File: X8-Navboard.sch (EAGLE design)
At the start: 14 parts, among them U1 MS5803-14BA

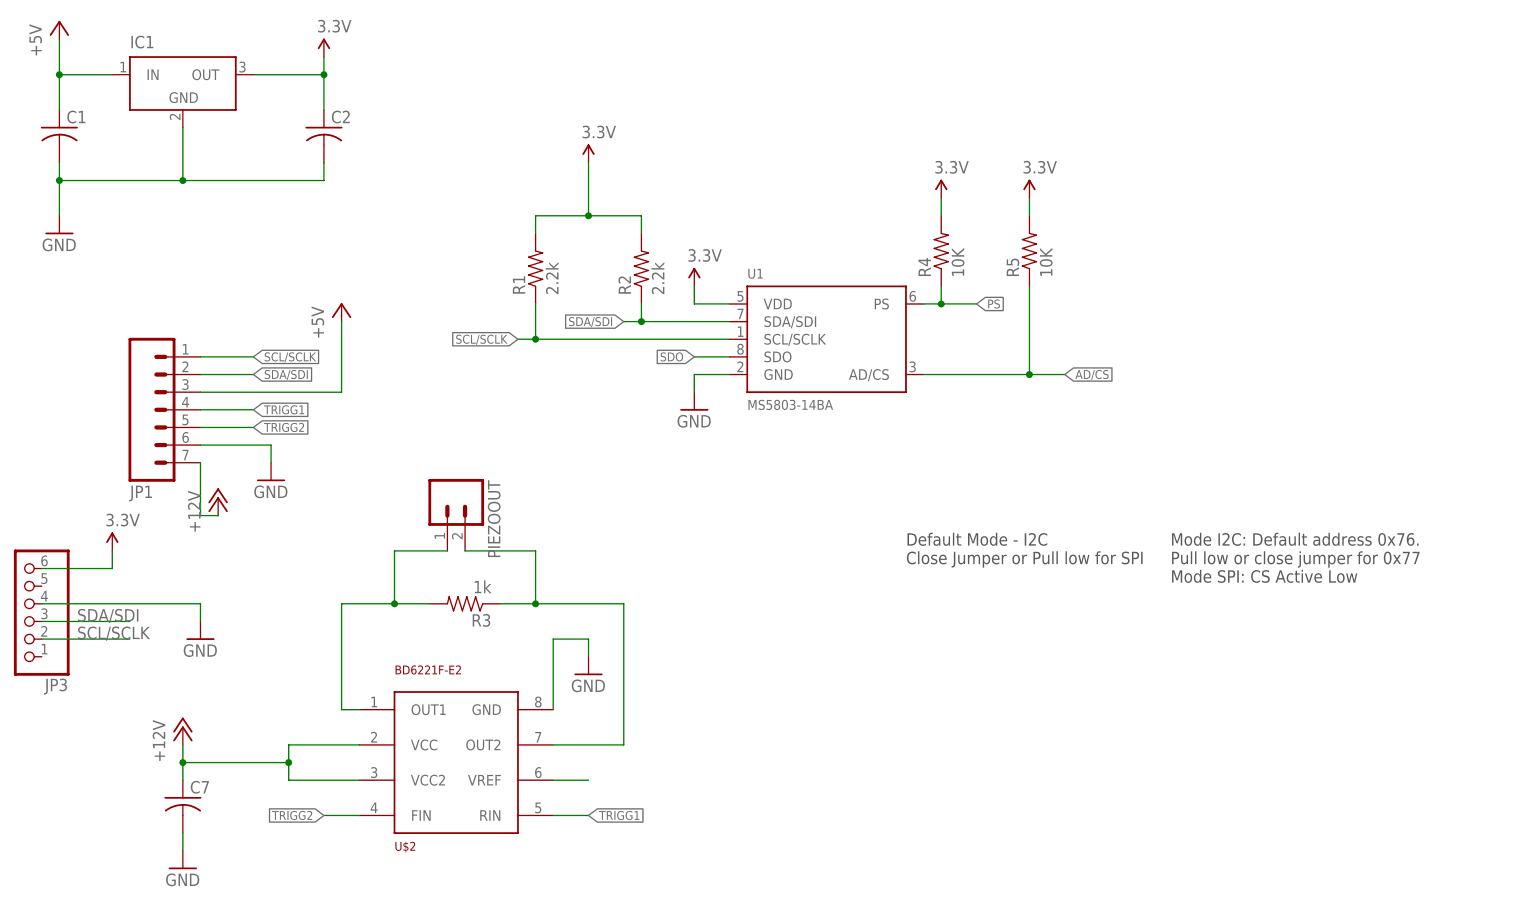
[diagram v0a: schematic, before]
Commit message: Finished the board layout for the nav board
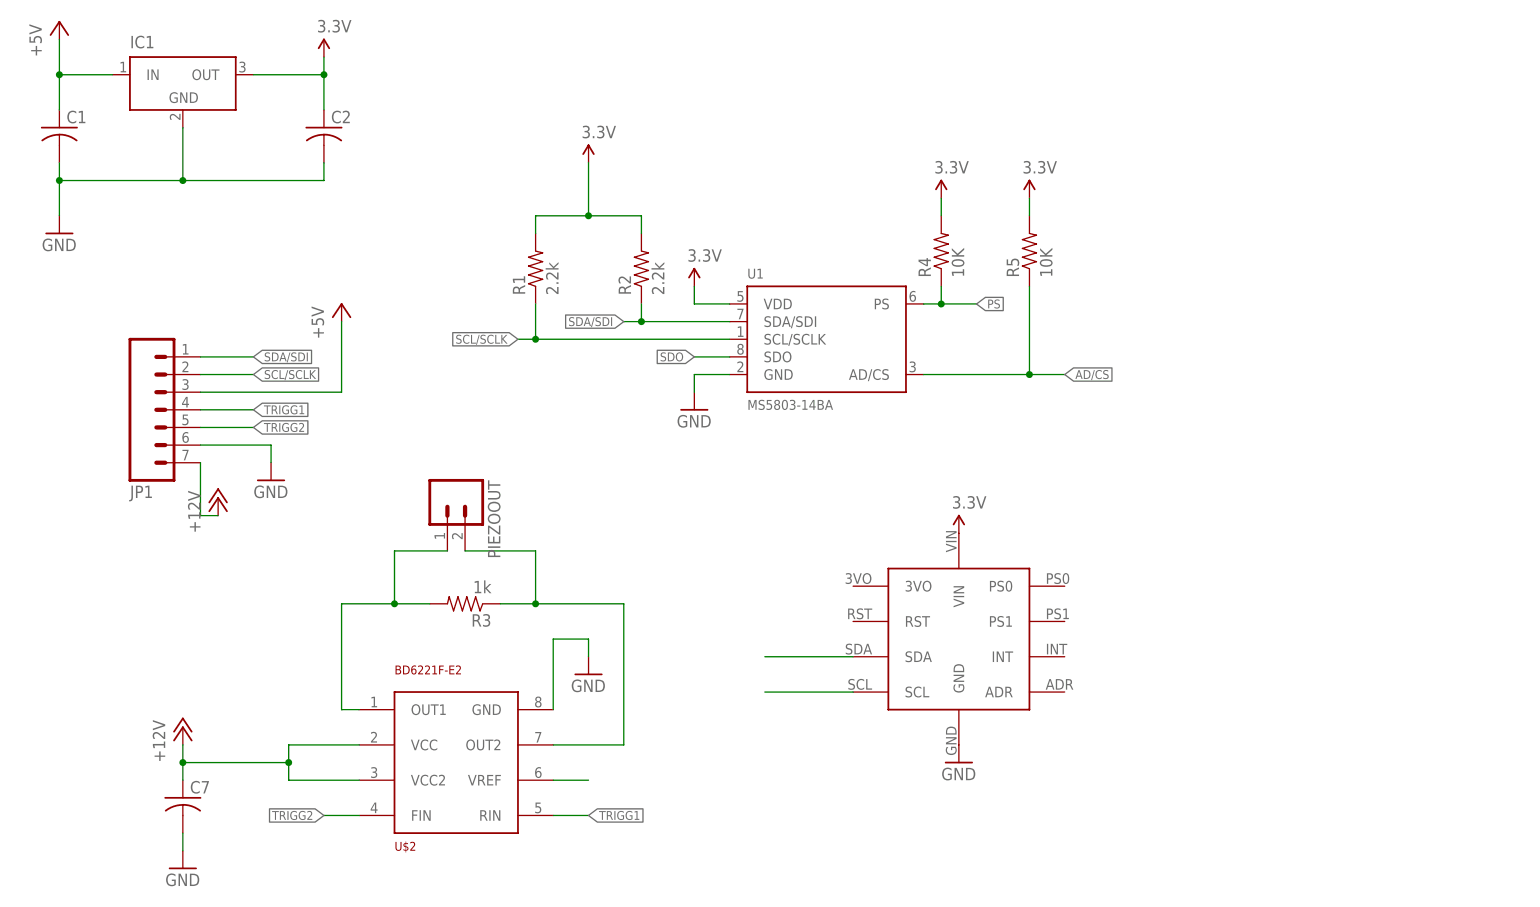
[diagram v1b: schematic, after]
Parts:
- removed JP3: (no value), pinhead:PINHD-1X6
- added U$1: BNO055_9DOF_BREAKOUT, Other:BNO055_9DOF_BREAKOUT
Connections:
- net 3.3V: now also U$1.VIN; no longer JP3.6
- net GND: now also U$1.GND; no longer JP3.4
- net SCL/SCLK: now also JP1.2, U$1.SCL; no longer JP1.1, JP3.2
- net SDA/SDI: now also JP1.1, U$1.SDA; no longer JP1.2, JP3.3
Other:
- note removed: "Default Mode - I2C Close Jumper or Pull low for SPI"
- note removed: "Mode I2C: Default address 0x76. Pull low or close jumper for 0x77 Mode SPI: CS Active Low"
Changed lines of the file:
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@@
 <part name="U$2" library="BNo-055" deviceset="BD6221F-E2" device=""/>
 <part name="PIEZOOUT" library="SparkFun-Connectors" deviceset="M02" device="LOCK_LONGPADS"/>
-<part name="SUPPLY9" library="SparkFun-Aesthetics" deviceset="3.3V" device=""/>
-<part name="GND10" library="SparkFun-Aesthetics" deviceset="GND" device=""/>
 <part name="P+1" library="supply1" deviceset="+5V" device=""/>
 <part name="P+2" library="supply1" deviceset="+5V" device=""/>
@@
 <part name="SUPPLY2" library="SparkFun-Aesthetics" deviceset="3.3V" device=""/>
 <part name="SUPPLY7" library="SparkFun-Aesthetics" deviceset="3.3V" device=""/>
-<part name="JP3" library="pinhead" deviceset="PINHD-1X6" device=""/>
+<part name="U$1" library="Other" deviceset="BNO055_9DOF_BREAKOUT" device=""/>
+<part name="SUPPLY3" library="SparkFun-Aesthetics" deviceset="3.3V" device=""/>
+<part name="GND5" library="SparkFun-Aesthetics" deviceset="GND" device=""/>
 </parts>
 <sheets>
 <sheet>
 <plain>
-<text x="157.48" y="86.36" size="1.778" layer="97" align="top-left">Default Mode - I2C
-Close Jumper or Pull low for SPI</text>
-<text x="195.58" y="86.36" size="1.778" layer="97" align="top-left">Mode I2C: Default address 0x76.
-Pull low or close jumper for 0x77
-Mode SPI: CS Active Low</text>
 </plain>
 <instances>
@@
 <instance part="U$2" gate="G$1" x="83.82" y="43.18"/>
 <instance part="PIEZOOUT" gate="G$1" x="91.44" y="91.44" rot="R270"/>
-<instance part="SUPPLY9" gate="G$1" x="43.18" y="83.82"/>
-<instance part="GND10" gate="1" x="55.88" y="71.12"/>
 <instance part="P+1" gate="1" x="35.56" y="160.02"/>
 <instance part="P+2" gate="1" x="76.2" y="119.38"/>
@@
 <instance part="SUPPLY2" gate="G$1" x="162.56" y="134.62"/>
 <instance part="SUPPLY7" gate="G$1" x="175.26" y="134.62"/>
-<instance part="JP3" gate="A" x="30.48" y="76.2" rot="R180"/>
+<instance part="U$1" gate="G$1" x="167.64" y="68.58"/>
+<instance part="SUPPLY3" gate="G$1" x="165.1" y="86.36"/>
+<instance part="GND5" gate="1" x="165.1" y="53.34"/>
 </instances>
 <busses>
@@
 </segment>
 <segment>
-<pinref part="JP3" gate="A" pin="6"/>
-<pinref part="SUPPLY9" gate="G$1" pin="3.3V"/>
-<wire x1="33.02" y1="81.28" x2="43.18" y2="81.28" width="0.1524" layer="91"/>
-<wire x1="43.18" y1="81.28" x2="43.18" y2="83.82" width="0.1524" layer="91"/>
+<pinref part="U$1" gate="G$1" pin="VIN"/>
+<pinref part="SUPPLY3" gate="G$1" pin="3.3V"/>
 </segment>
 </net>
@@
 </segment>
 <segment>
-<pinref part="JP3" gate="A" pin="4"/>
-<pinref part="GND10" gate="1" pin="GND"/>
-<wire x1="33.02" y1="76.2" x2="55.88" y2="76.2" width="0.1524" layer="91"/>
-<wire x1="55.88" y1="76.2" x2="55.88" y2="73.66" width="0.1524" layer="91"/>
+<pinref part="U$1" gate="G$1" pin="GND"/>
+<pinref part="GND5" gate="1" pin="GND"/>
 </segment>
 </net>
 <net name="SDA/SDI" class="0">
 <segment>
-<wire x1="45.72" y1="73.66" x2="33.02" y2="73.66" width="0.1524" layer="91"/>
-<label x="38.1" y="73.66" size="1.778" layer="95"/>
-<pinref part="JP3" gate="A" pin="3"/>
-</segment>
-<segment>
-<pinref part="JP1" gate="G$1" pin="2"/>
-<wire x1="55.88" y1="109.22" x2="63.5" y2="109.22" width="0.1524" layer="91"/>
-<label x="63.5" y="109.22" size="1.27" layer="95" xref="yes"/>
+<label x="63.5" y="111.76" size="1.27" layer="95" xref="yes"/>
+<wire x1="63.5" y1="111.76" x2="55.88" y2="111.76" width="0.1524" layer="91"/>
+<pinref part="JP1" gate="G$1" pin="1"/>
 </segment>
 <segment>
@@
 <label x="116.84" y="116.84" size="1.27" layer="95" rot="R180" xref="yes"/>
 </segment>
+<segment>
+<wire x1="149.86" y1="68.58" x2="137.16" y2="68.58" width="0.1524" layer="91"/>
+<pinref part="U$1" gate="G$1" pin="SDA"/>
+</segment>
 </net>
 <net name="SCL/SCLK" class="0">
 <segment>
-<wire x1="45.72" y1="71.12" x2="33.02" y2="71.12" width="0.1524" layer="91"/>
-<label x="38.1" y="71.12" size="1.778" layer="95"/>
-<pinref part="JP3" gate="A" pin="2"/>
-</segment>
-<segment>
-<pinref part="JP1" gate="G$1" pin="1"/>
-<wire x1="55.88" y1="111.76" x2="63.5" y2="111.76" width="0.1524" layer="91"/>
-<label x="63.5" y="111.76" size="1.27" layer="95" xref="yes"/>
+<label x="63.5" y="109.22" size="1.27" layer="95" xref="yes"/>
+<pinref part="JP1" gate="G$1" pin="2"/>
+<wire x1="55.88" y1="109.22" x2="63.5" y2="109.22" width="0.1524" layer="91"/>
 </segment>
 <segment>
@@
 <junction x="104.14" y="114.3"/>
 <label x="101.6" y="114.3" size="1.27" layer="95" rot="R180" xref="yes"/>
+</segment>
+<segment>
+<wire x1="149.86" y1="63.5" x2="137.16" y2="63.5" width="0.1524" layer="91"/>
+<pinref part="U$1" gate="G$1" pin="SCL"/>
 </segment>
 </net>
@@
 </schematic>
 </drawing>
-<compatibility>
-<note version="6.3" minversion="6.2.2" severity="warning">
-Since Version 6.2.2 text objects can contain more than one line,
-which will not be processed correctly with this version.
-</note>
-</compatibility>
 </eagle>
